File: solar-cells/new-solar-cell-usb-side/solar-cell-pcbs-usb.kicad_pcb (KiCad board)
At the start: 2 copper layers, 80 x 103.5 mm, 16 parts, among them J1 Solar Cell

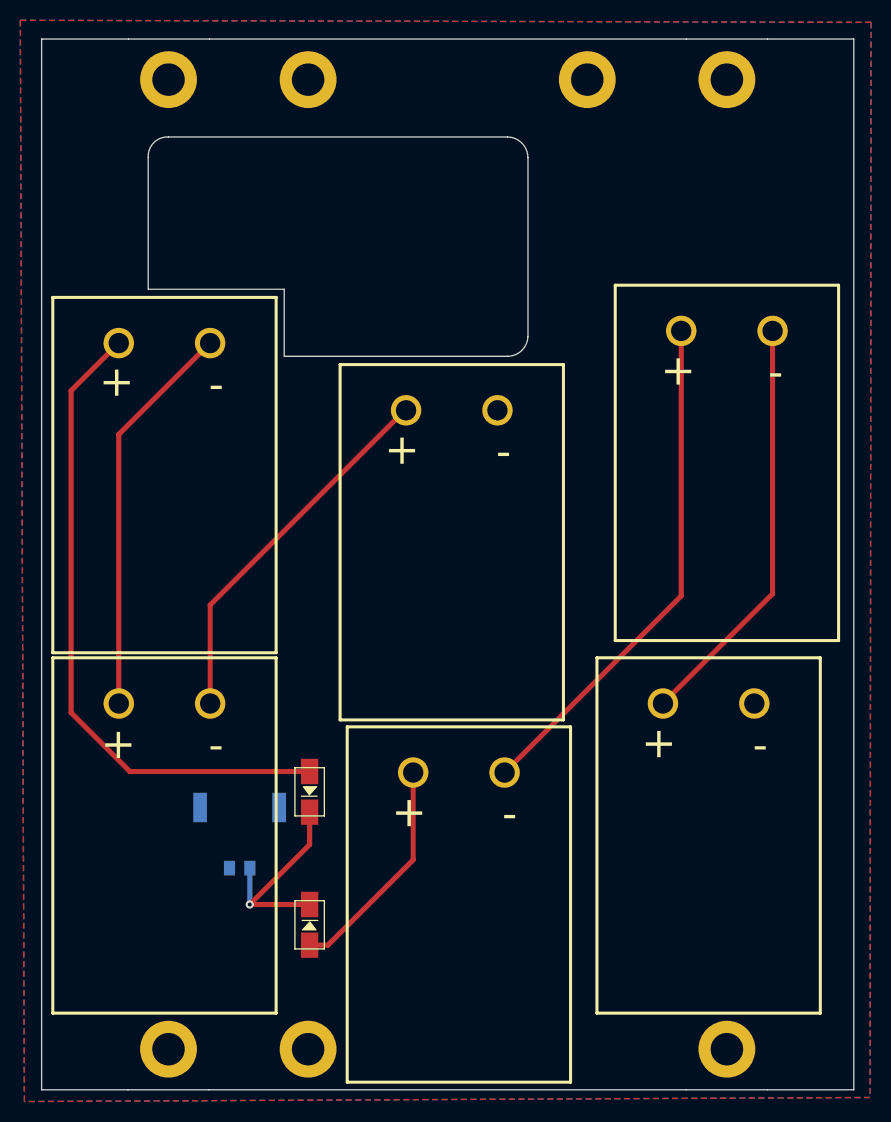
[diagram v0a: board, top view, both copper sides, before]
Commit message: fixed tracks, added vias
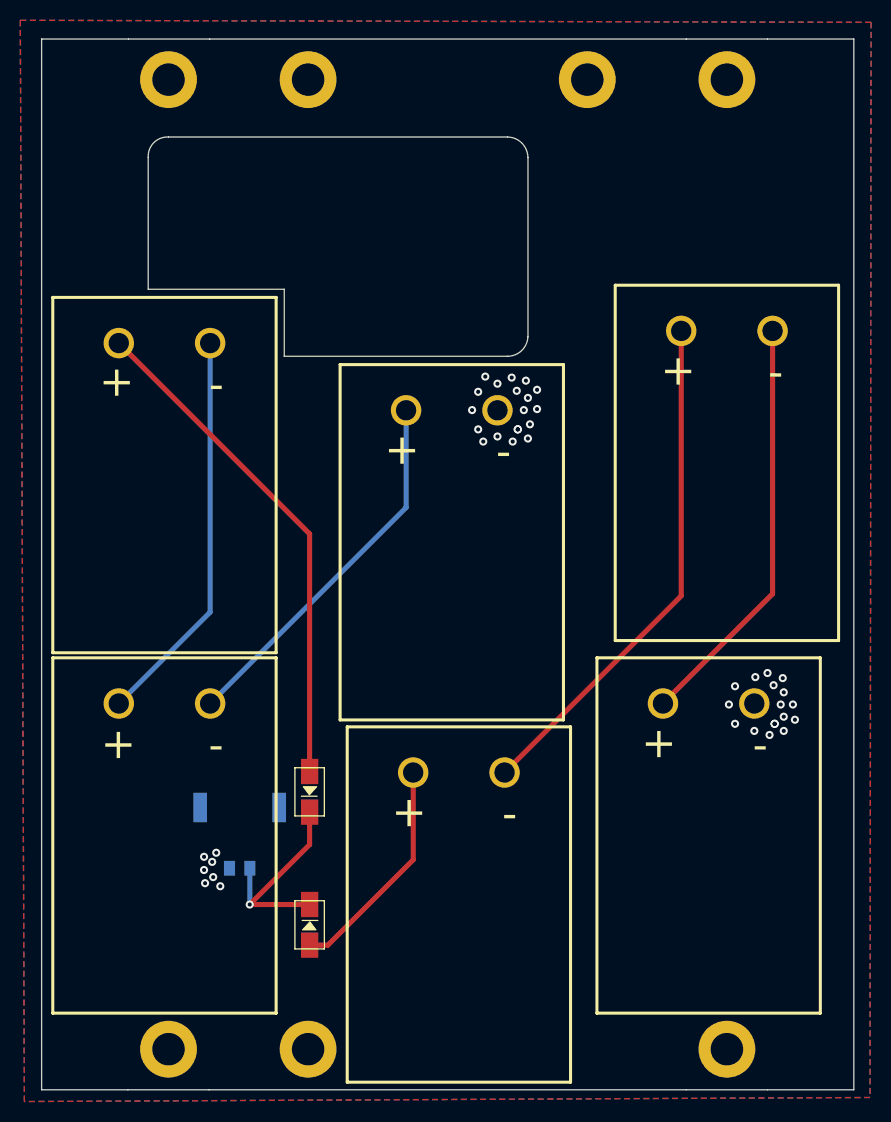
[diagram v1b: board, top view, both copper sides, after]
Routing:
- net Net-(D2-Pad2): track 64.2 -> 50.0 mm
- net GND: vias 0 -> 43
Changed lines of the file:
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@@
     (style (thickness 0.15) (arrow_length 1.27) (text_position_mode 0) (extension_height 0.58642) (extension_offset 0.5) keep_text_aligned)
   )
+  (via (at 146.1 104.3) (size 0.8) (drill 0.4) (layers "F.Cu" "B.Cu") (free) (net 1))
+  (via (at 145.2 106.9) (size 0.8) (drill 0.4) (layers "F.Cu" "B.Cu") (free) (net 1))
+  (via (at 144.3 106.2) (size 0.8) (drill 0.4) (layers "F.Cu" "B.Cu") (free) (net 1))
+  (via (at 142.4 101.6) (size 0.8) (drill 0.4) (layers "F.Cu" "B.Cu") (free) (net 1))
+  (via (at 120 78.1) (size 0.8) (drill 0.4) (layers "F.Cu" "B.Cu") (free) (net 1))
+  (via (at 144.2 102.4) (size 0.8) (drill 0.4) (layers "F.Cu" "B.Cu") (free) (net 1))
+  (via (at 120.9 73.3) (size 0.8) (drill 0.4) (layers "F.Cu" "B.Cu") (free) (net 1))
+  (via (at 140.4 102.5) (size 0.8) (drill 0.4) (layers "F.Cu" "B.Cu") (free) (net 1))
+  (via (at 117 77.9) (size 0.8) (drill 0.4) (layers "F.Cu" "B.Cu") (free) (net 1))
+  (via (at 118.4 72.1) (size 0.8) (drill 0.4) (layers "F.Cu" "B.Cu") (free) (net 1))
+  (via (at 120.9 75.2) (size 0.8) (drill 0.4) (layers "F.Cu" "B.Cu") (free) (net 1))
+  (via (at 115.6 78.4) (size 0.8) (drill 0.4) (layers "F.Cu" "B.Cu") (free) (net 1))
+  (via (at 118.9 73.4) (size 0.8) (drill 0.4) (layers "F.Cu" "B.Cu") (free) (net 1))
+  (via (at 89.3 118.9) (size 0.8) (drill 0.4) (layers "F.Cu" "B.Cu") (free) (net 1))
+  (via (at 88.1 120.6) (size 0.8) (drill 0.4) (layers "F.Cu" "B.Cu") (free) (net 1))
+  (via (at 114.5 75.3) (size 0.8) (drill 0.4) (layers "F.Cu" "B.Cu") (free) (net 1))
+  (via (at 144.3 106.2) (size 0.8) (drill 0.4) (layers "F.Cu" "B.Cu") (free) (net 1))
+  (via (at 115.1 73.5) (size 0.8) (drill 0.4) (layers "F.Cu" "B.Cu") (free) (net 1))
+  (via (at 142.3 106.9) (size 0.8) (drill 0.4) (layers "F.Cu" "B.Cu") (free) (net 1))
+  (via (at 120.2 76.7) (size 0.8) (drill 0.4) (layers "F.Cu" "B.Cu") (free) (net 1))
+  (via (at 119 77.2) (size 0.8) (drill 0.4) (layers "F.Cu" "B.Cu") (free) (net 1))
+  (via (at 88.2 121.9) (size 0.8) (drill 0.4) (layers "F.Cu" "B.Cu") (free) (net 1))
+  (via (at 119.6 75.3) (size 0.8) (drill 0.4) (layers "F.Cu" "B.Cu") (free) (net 1))
+  (via (at 89 121.3) (size 0.8) (drill 0.4) (layers "F.Cu" "B.Cu") (free) (net 1))
+  (via (at 145.2 105.5) (size 0.8) (drill 0.4) (layers "F.Cu" "B.Cu") (free) (net 1))
+  (via (at 120 74.1) (size 0.8) (drill 0.4) (layers "F.Cu" "B.Cu") (free) (net 1))
+  (via (at 88.1 119.3) (size 0.8) (drill 0.4) (layers "F.Cu" "B.Cu") (free) (net 1))
+  (via (at 144.9 104.3) (size 0.8) (drill 0.4) (layers "F.Cu" "B.Cu") (free) (net 1))
+  (via (at 115.8 72) (size 0.8) (drill 0.4) (layers "F.Cu" "B.Cu") (free) (net 1))
+  (via (at 140.4 106.2) (size 0.8) (drill 0.4) (layers "F.Cu" "B.Cu") (free) (net 1))
+  (via (at 119 77.2) (size 0.8) (drill 0.4) (layers "F.Cu" "B.Cu") (free) (net 1))
+  (via (at 88.9 119.8) (size 0.8) (drill 0.4) (layers "F.Cu" "B.Cu") (free) (net 1))
+  (via (at 117 72.7) (size 0.8) (drill 0.4) (layers "F.Cu" "B.Cu") (free) (net 1))
+  (via (at 118.5 78.4) (size 0.8) (drill 0.4) (layers "F.Cu" "B.Cu") (free) (net 1))
+  (via (at 139.8 104.3) (size 0.8) (drill 0.4) (layers "F.Cu" "B.Cu") (free) (net 1))
+  (via (at 145.2 103.1) (size 0.8) (drill 0.4) (layers "F.Cu" "B.Cu") (free) (net 1))
+  (via (at 115.1 77.2) (size 0.8) (drill 0.4) (layers "F.Cu" "B.Cu") (free) (net 1))
+  (via (at 89.7 122.2) (size 0.8) (drill 0.4) (layers "F.Cu" "B.Cu") (free) (net 1))
+  (via (at 143.8 107.3) (size 0.8) (drill 0.4) (layers "F.Cu" "B.Cu") (free) (net 1))
+  (via (at 119.8 72.4) (size 0.8) (drill 0.4) (layers "F.Cu" "B.Cu") (free) (net 1))
+  (via (at 145.1 101.7) (size 0.8) (drill 0.4) (layers "F.Cu" "B.Cu") (free) (net 1))
+  (via (at 143.6 101.2) (size 0.8) (drill 0.4) (layers "F.Cu" "B.Cu") (free) (net 1))
+  (via (at 146.3 105.8) (size 0.8) (drill 0.4) (layers "F.Cu" "B.Cu") (free) (net 1))
   (segment (start 135.1 93.6) (end 117.7 111) (width 0.5) (layer "F.Cu") (net 2))
   (segment (start 135.1 67.5) (end 135.1 93.6) (width 0.5) (layer "F.Cu") (net 2))
@@
   (segment (start 108.7 119.6) (end 108.7 111) (width 0.5) (layer "F.Cu") (net 3))
   (segment (start 100.3 128) (end 108.7 119.6) (width 0.5) (layer "F.Cu") (net 3))
-  (segment (start 79.7 68.7) (end 75 73.4) (width 0.5) (layer "F.Cu") (net 4))
-  (segment (start 80.8 110.9) (end 98.5 110.9) (width 0.5) (layer "F.Cu") (net 4))
-  (segment (start 75 105.1) (end 80.8 110.9) (width 0.5) (layer "F.Cu") (net 4))
-  (segment (start 75 73.4) (end 75 105.1) (width 0.5) (layer "F.Cu") (net 4))
+  (segment (start 79.7 68.7) (end 98.5 87.5) (width 0.5) (layer "F.Cu") (net 4))
+  (segment (start 98.5 87.5) (end 98.5 110.9) (width 0.5) (layer "F.Cu") (net 4))
   (segment (start 144.1 93.4) (end 133.3 104.2) (width 0.5) (layer "F.Cu") (net 5))
   (segment (start 144.1 67.5) (end 144.1 93.4) (width 0.5) (layer "F.Cu") (net 5))
-  (segment (start 79.7 77.7) (end 79.7 104.2) (width 0.5) (layer "F.Cu") (net 6))
-  (segment (start 88.7 68.7) (end 79.7 77.7) (width 0.5) (layer "F.Cu") (net 6))
-  (segment (start 107.88 75.32) (end 88.7 94.5) (width 0.5) (layer "F.Cu") (net 7))
-  (segment (start 88.7 94.5) (end 88.7 104.2) (width 0.5) (layer "F.Cu") (net 7))
+  (segment (start 88.7 68.7) (end 88.7 95.2) (width 0.5) (layer "B.Cu") (net 6))
+  (segment (start 88.7 95.2) (end 79.7 104.2) (width 0.5) (layer "B.Cu") (net 6))
   (segment (start 108 75.32) (end 107.88 75.32) (width 0.25) (layer "F.Cu") (net 7))
+  (segment (start 108 84.9) (end 88.7 104.2) (width 0.5) (layer "B.Cu") (net 7))
+  (segment (start 108 75.32) (end 108 84.9) (width 0.5) (layer "B.Cu") (net 7))
   (segment (start 92.6 124) (end 98.5 124) (width 0.5) (layer "F.Cu") (net 8))
   (segment (start 92.6 124) (end 98.5 118.1) (width 0.5) (layer "F.Cu") (net 8))
